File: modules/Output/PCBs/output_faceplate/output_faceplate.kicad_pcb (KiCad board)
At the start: 2 copper layers, 40.3 x 128.5 mm, 0 parts

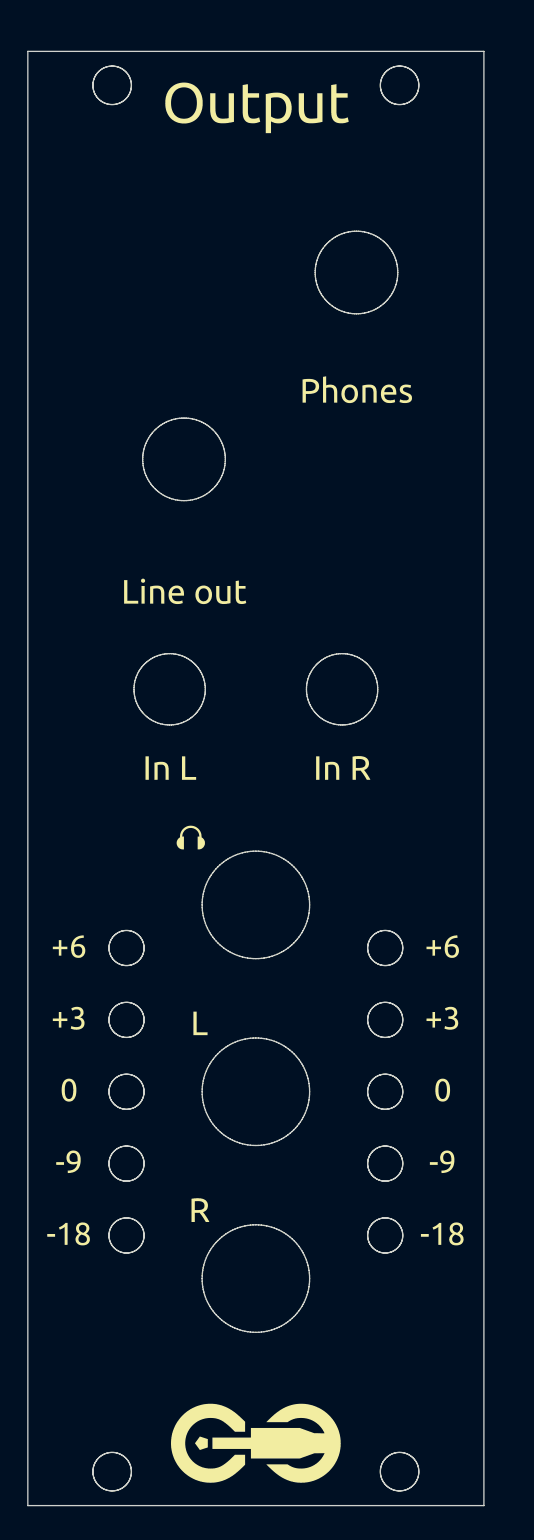
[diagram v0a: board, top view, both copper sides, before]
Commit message: add copper to output faceplate
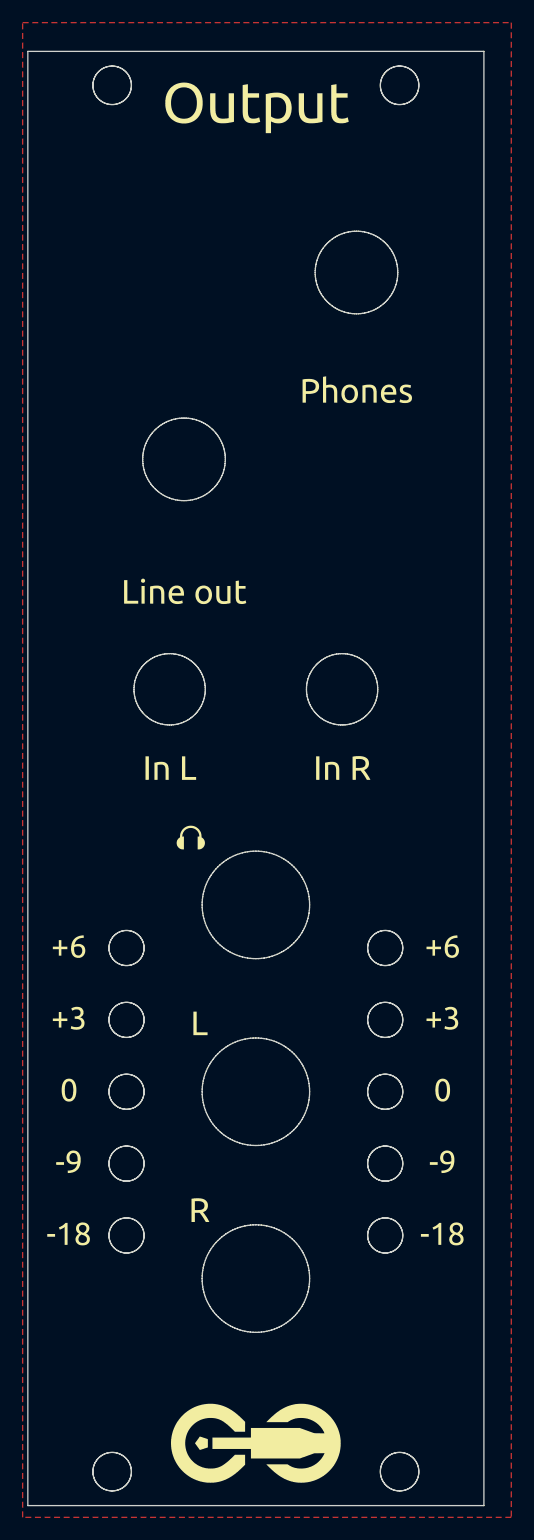
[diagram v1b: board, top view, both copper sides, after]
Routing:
- added copper zone on F.Cu, net (none)
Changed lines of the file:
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@@
       (xy 54.899999 70.499994)
     )
-    (stroke (width 0) (type solid)) (fill none) (layer "Edge.Cuts"))
+    (stroke (width 0.1) (type solid)) (fill none) (layer "Edge.Cuts"))
   (gr_poly
     (pts
@@
       (xy 49.819999 134.829992)
     )
-    (stroke (width 0) (type solid)) (fill none) (layer "Edge.Cuts"))
+    (stroke (width 0.1) (type solid)) (fill none) (layer "Edge.Cuts"))
   (gr_poly
     (pts
@@
       (xy 70.139999 53.99)
     )
-    (stroke (width 0) (type solid)) (fill none) (layer "Edge.Cuts"))
+    (stroke (width 0.1) (type solid)) (fill none) (layer "Edge.Cuts"))
   (gr_poly
     (pts
@@
       (xy 49.819999 141.17999)
     )
-    (stroke (width 0) (type solid)) (fill none) (layer "Edge.Cuts"))
+    (stroke (width 0.1) (type solid)) (fill none) (layer "Edge.Cuts"))
   (gr_poly
     (pts
@@
       (xy 48.549999 39.4)
     )
-    (stroke (width 0) (type solid)) (fill none) (layer "Edge.Cuts"))
+    (stroke (width 0.1) (type solid)) (fill none) (layer "Edge.Cuts"))
   (gr_poly
     (pts
@@
       (xy 72.679998 122.129995)
     )
-    (stroke (width 0) (type solid)) (fill none) (layer "Edge.Cuts"))
+    (stroke (width 0.1) (type solid)) (fill none) (layer "Edge.Cuts"))
   (gr_poly
     (pts
@@
       (xy 73.949995 161.899999)
     )
-    (stroke (width 0) (type solid)) (fill none) (layer "Edge.Cuts"))
+    (stroke (width 0.1) (type solid)) (fill none) (layer "Edge.Cuts"))
   (gr_poly
     (pts
@@
       (xy 61.249998 125.279996)
     )
-    (stroke (width 0) (type solid)) (fill none) (layer "Edge.Cuts"))
+    (stroke (width 0.1) (type solid)) (fill none) (layer "Edge.Cuts"))
   (gr_poly
     (pts
@@
       (xy 72.679998 141.17999)
     )
-    (stroke (width 0) (type solid)) (fill none) (layer "Edge.Cuts"))
+    (stroke (width 0.1) (type solid)) (fill none) (layer "Edge.Cuts"))
   (gr_poly
     (pts
@@
       (xy 53.629999 91.319993)
     )
-    (stroke (width 0) (type solid)) (fill none) (layer "Edge.Cuts"))
+    (stroke (width 0.1) (type solid)) (fill none) (layer "Edge.Cuts"))
   (gr_poly
     (pts
@@
       (xy 49.819999 128.479993)
     )
-    (stroke (width 0) (type solid)) (fill none) (layer "Edge.Cuts"))
+    (stroke (width 0.1) (type solid)) (fill none) (layer "Edge.Cuts"))
   (gr_poly
     (pts
@@
       (xy 49.819999 122.129995)
     )
-    (stroke (width 0) (type solid)) (fill none) (layer "Edge.Cuts"))
+    (stroke (width 0.1) (type solid)) (fill none) (layer "Edge.Cuts"))
   (gr_poly
     (pts
@@
       (xy 61.249998 108.769994)
     )
-    (stroke (width 0) (type solid)) (fill none) (layer "Edge.Cuts"))
+    (stroke (width 0.1) (type solid)) (fill none) (layer "Edge.Cuts"))
   (gr_poly
     (pts
@@
       (xy 72.679998 128.479993)
     )
-    (stroke (width 0) (type solid)) (fill none) (layer "Edge.Cuts"))
+    (stroke (width 0.1) (type solid)) (fill none) (layer "Edge.Cuts"))
   (gr_poly
     (pts
@@
       (xy 68.869999 91.319993)
     )
-    (stroke (width 0) (type solid)) (fill none) (layer "Edge.Cuts"))
+    (stroke (width 0.1) (type solid)) (fill none) (layer "Edge.Cuts"))
   (gr_poly
     (pts
@@
       (xy 48.549999 161.899999)
     )
-    (stroke (width 0) (type solid)) (fill none) (layer "Edge.Cuts"))
+    (stroke (width 0.1) (type solid)) (fill none) (layer "Edge.Cuts"))
   (gr_poly
     (pts
@@
       (xy 73.949995 39.4)
     )
-    (stroke (width 0) (type solid)) (fill none) (layer "Edge.Cuts"))
+    (stroke (width 0.1) (type solid)) (fill none) (layer "Edge.Cuts"))
   (gr_poly
     (pts
@@
       (xy 72.679998 134.829992)
     )
-    (stroke (width 0) (type solid)) (fill none) (layer "Edge.Cuts"))
+    (stroke (width 0.1) (type solid)) (fill none) (layer "Edge.Cuts"))
   (gr_poly
     (pts
@@
       (xy 49.819999 115.779996)
     )
-    (stroke (width 0) (type solid)) (fill none) (layer "Edge.Cuts"))
+    (stroke (width 0.1) (type solid)) (fill none) (layer "Edge.Cuts"))
   (gr_poly
     (pts
@@
       (xy 72.679998 115.779996)
     )
-    (stroke (width 0) (type solid)) (fill none) (layer "Edge.Cuts"))
+    (stroke (width 0.1) (type solid)) (fill none) (layer "Edge.Cuts"))
   (gr_poly
     (pts
@@
       (xy 81.399995 38.1)
     )
-    (stroke (width 0) (type solid)) (fill none) (layer "Edge.Cuts"))
+    (stroke (width 0.1) (type solid)) (fill none) (layer "Edge.Cuts"))
   (gr_poly
     (pts
@@
       (xy 61.249998 141.789998)
     )
-    (stroke (width 0) (type solid)) (fill none) (layer "Edge.Cuts"))
+    (stroke (width 0.1) (type solid)) (fill none) (layer "Edge.Cuts"))
+  (zone (net 0) (net_name "") (layer "F.Cu") (hatch edge 0.5)
+    (connect_pads (clearance 0.5))
+    (min_thickness 0.25) (filled_areas_thickness no)
+    (fill yes (thermal_gap 0.5) (thermal_bridge_width 0.5) (island_removal_mode 1) (island_area_min 9.999999))
+    (polygon
+      (pts
+        (xy 40.64 35.56)
+        (xy 83.82 35.56)
+        (xy 83.82 167.64)
+        (xy 40.64 167.64)
+      )
+    )
+  )
   (group "" (id afebf451-df46-4a42-878e-d55b6b8dd718)
     (members
@@
       3795e62a-637d-4a98-bf3a-b120592b46a7
       3a0723c8-7afd-479d-9996-5c33899deb0d
-      3e149e67-6f02-41b2-a080-dc9f08e889c5
       3f4ce7b7-2910-4ee6-9fcd-e288206bcff0
       411d00d3-bd81-45fa-b917-79e09ec8bff4
@@
       7683941d-1a95-4752-83fb-fabfc4628b1d
       78f25892-a574-443c-970d-6545c3456a23
-      7f917b05-d999-44bb-a2a3-5e98f9b2f603
       81d2ae47-aa91-490b-a347-ee34e638d74f
       873deaf7-33ba-4475-ae4a-cdbd43d94a20

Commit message: remove copper from output faceplate
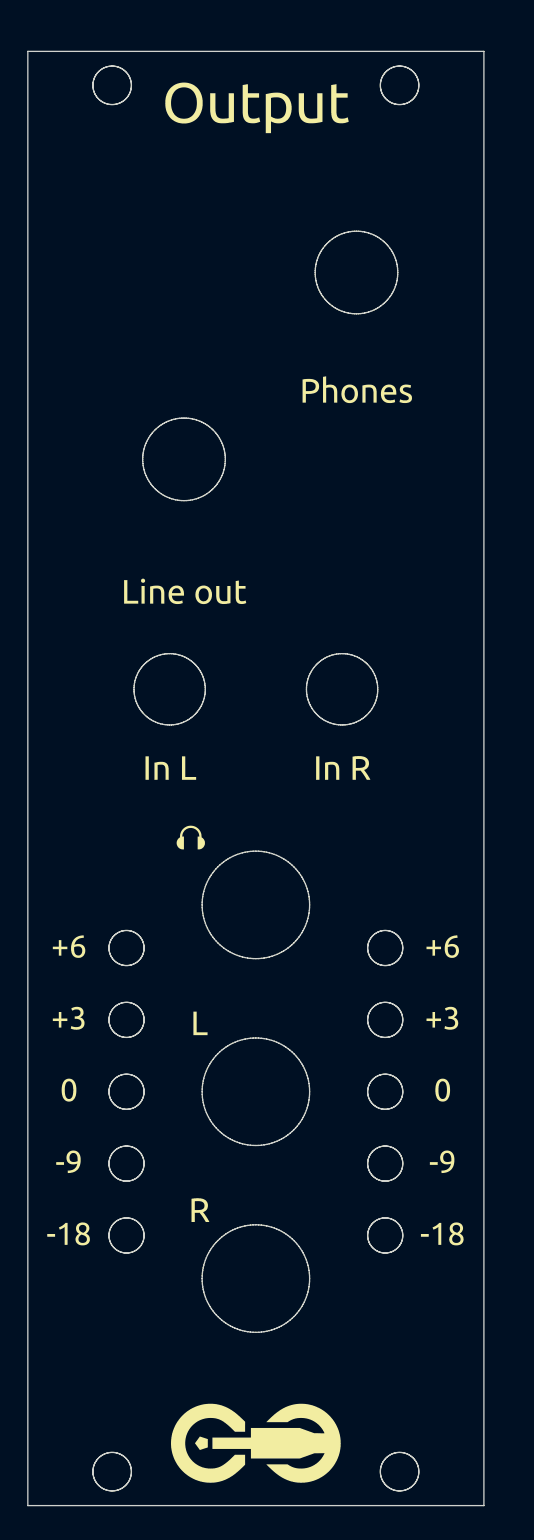
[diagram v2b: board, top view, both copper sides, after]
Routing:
- removed copper zone on F.Cu, net (none)
